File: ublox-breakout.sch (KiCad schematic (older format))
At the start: 43 parts, among them J1 Conn_02x06_Odd_Even, J2 Conn_Coaxial, J3 Conn_Coaxial, J4 USB_B_Micro, U1 74HCT2G125DP,125, U2 UBLOX_LEA-M8T-0, U3 TPUSBLC6-2SC6, U4 XC6206P332MR

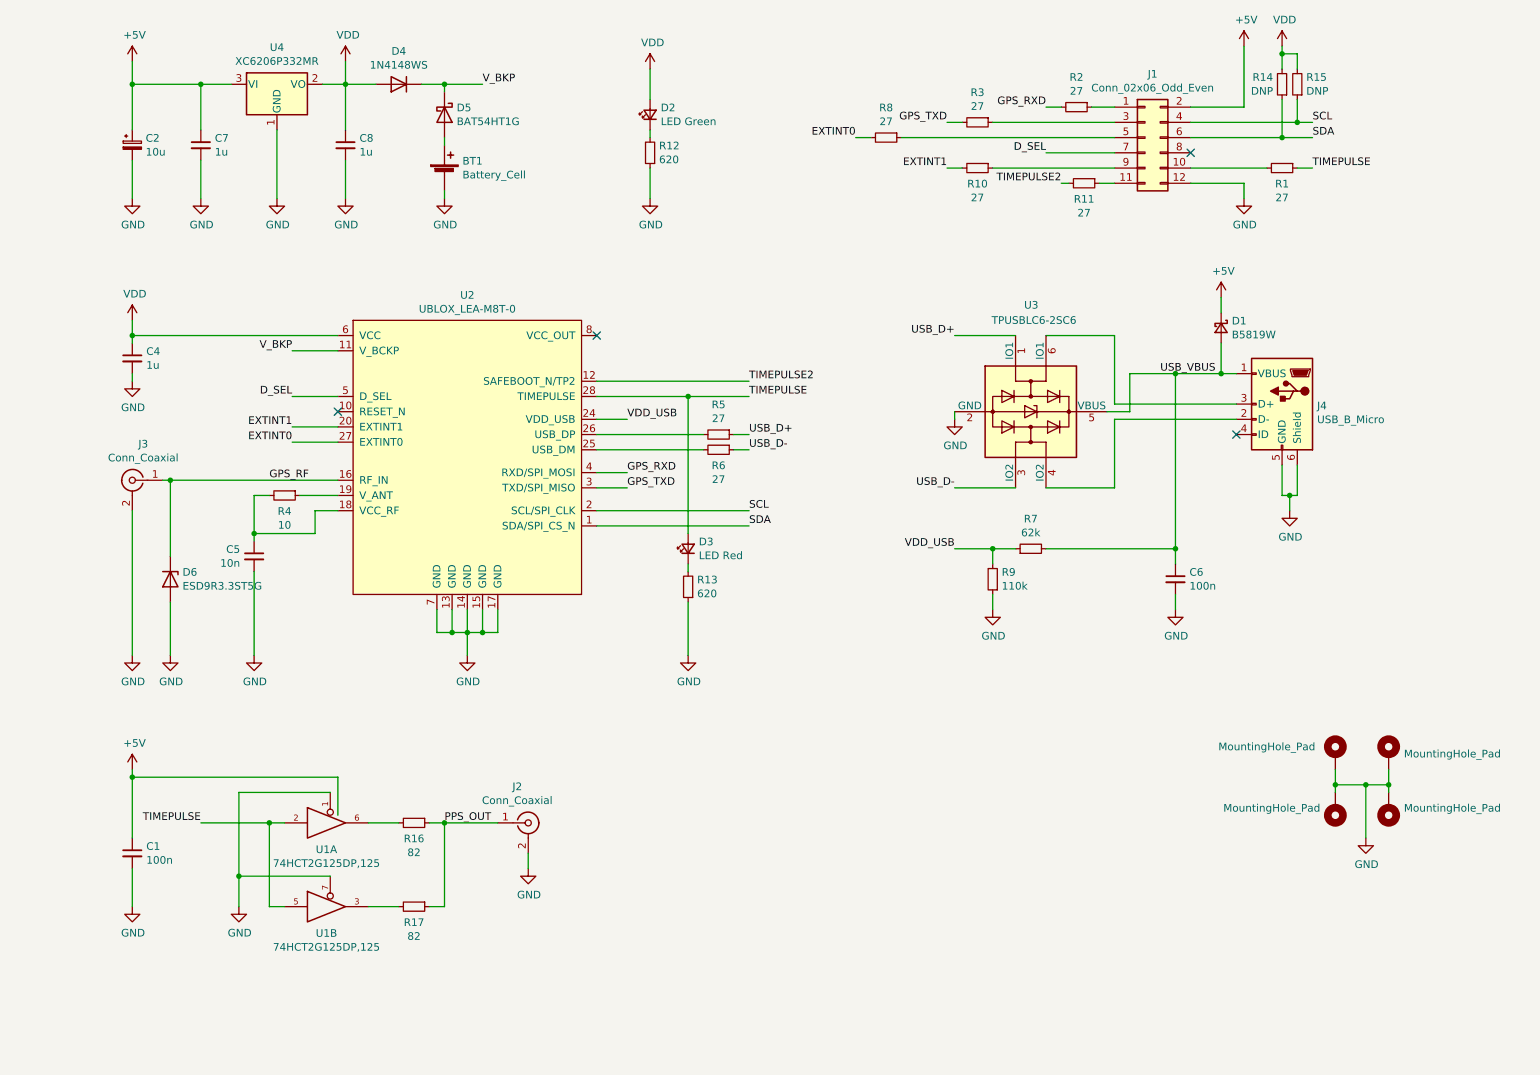
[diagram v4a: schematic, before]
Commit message: Fix USB and other issues
- use an LDO to provide VDD_USB as per HIM (major issue)
- correct trace width for GPS antenna input (minor issue)
- add OSHW logo on top silk
- add copyright notice on top silk
- update gerber, BOM and CPL files
- update schematic PDF
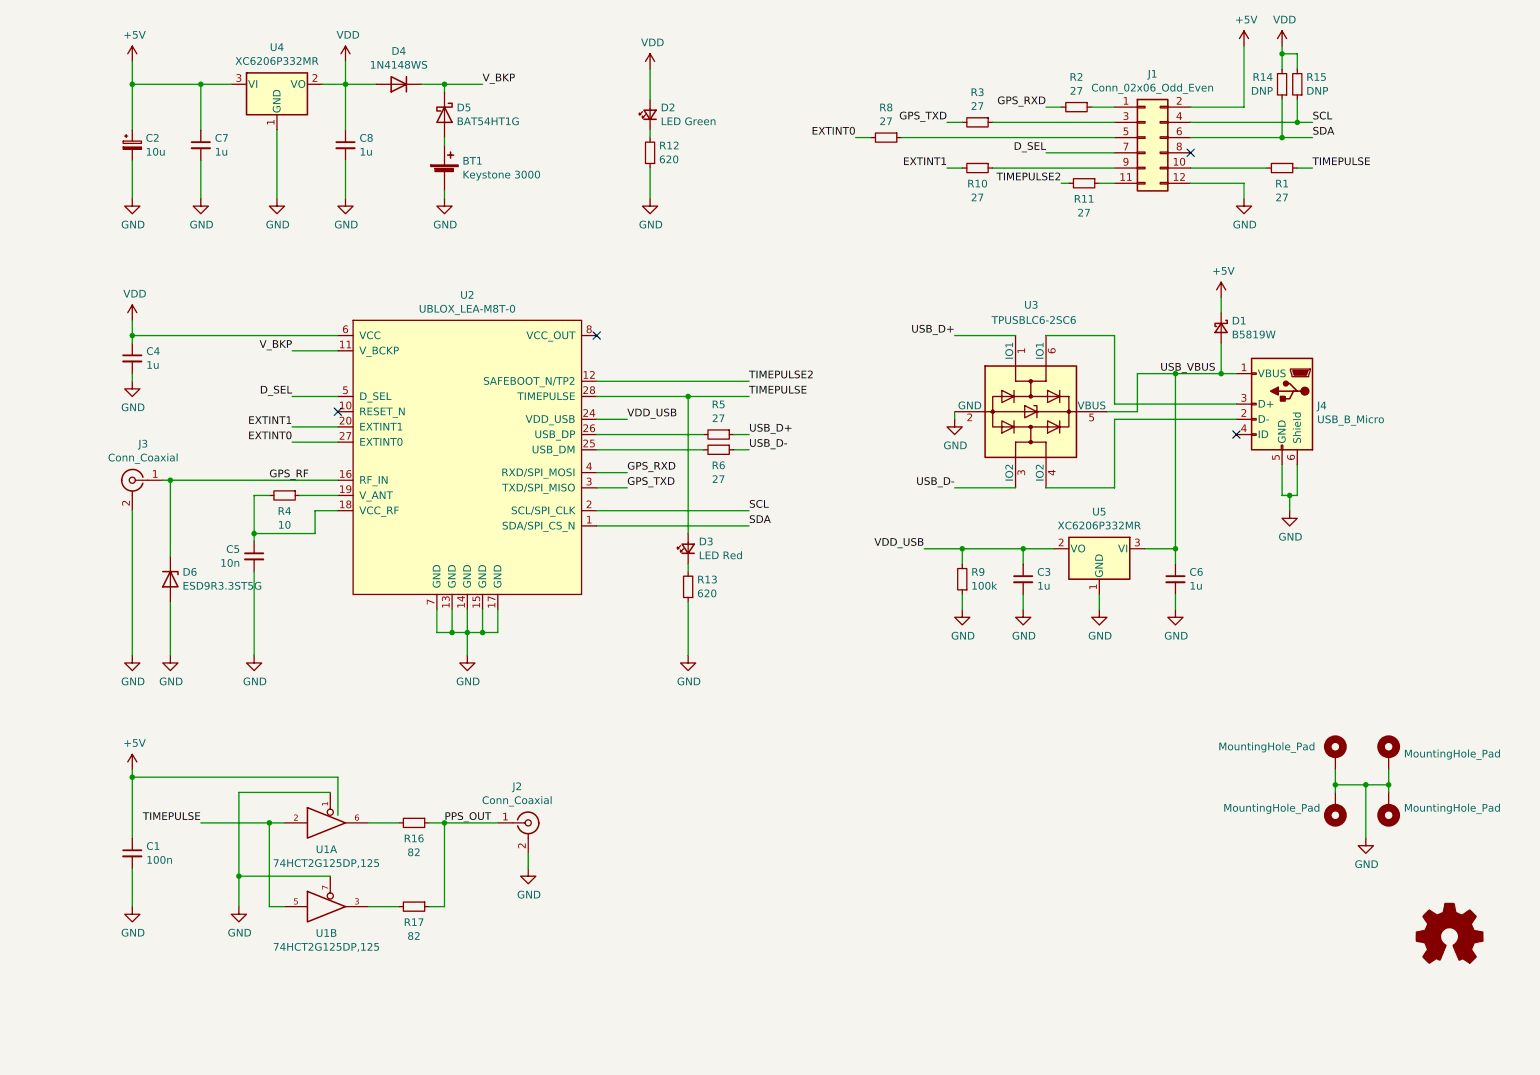
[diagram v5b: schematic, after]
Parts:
- removed R7: 62k, Resistor_SMD:R_0603_1608Metric, symbol Device:R_Small
- added C3: 1u, Capacitor_SMD:C_0603_1608Metric, symbol Device:C_Small
- added OSHW1: Logo_Open_Hardware_Small, Symbol:OSHW-Logo2_9.8x8mm_SilkScreen, symbol Graphic:Logo_Open_Hardware_Small
- added U5: XC6206P332MR, Package_TO_SOT_SMD:SOT-23, symbol Regulator_Linear:XC6206PxxxMR
- BT1: value Battery_Cell -> Keystone 3000
- C6: value 100n -> 1u; JLCPN C14663 -> C15849
- R9: value 110k -> 100k; JLCPN C25805 -> C25803
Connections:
- net GND: now also C3.2, U5.1 (GND)
- net USB_VBUS: now also U5.3 (VI)
- net VDD_USB: now also C3.1, U5.2 (VO)
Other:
- moved on the sheet: R9
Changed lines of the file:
@@
 	9250 3350 8450 3350
 Wire Wire Line
-	8550 3400 8400 3400
-Wire Wire Line
-	8550 3150 8550 3400
+	8600 3400 8400 3400
+Wire Wire Line
+	8600 3150 8600 3400
 Wire Wire Line
 	9250 3150 9150 3150
@@
 L Device:R_Small R9
 U 1 1 5FF28B14
-P 7650 4500
-F 0 "R9" H 7591 4454 50  0000 R CNN
-F 1 "110k" H 7591 4545 50  0000 R CNN
-F 2 "Resistor_SMD:R_0603_1608Metric" H 7650 4500 50  0001 C CNN
-F 3 "~" H 7650 4500 50  0001 C CNN
-F 4 "C25805" H 7650 4500 50  0001 C CNN "JLCPN"
-	1    7650 4500
+P 7450 4500
+F 0 "R9" H 7391 4454 50  0000 R CNN
+F 1 "100k" H 7391 4545 50  0000 R CNN
+F 2 "Resistor_SMD:R_0603_1608Metric" H 7450 4500 50  0001 C CNN
+F 3 "~" H 7450 4500 50  0001 C CNN
+F 4 "C25803" H 7450 4500 50  0001 C CNN "JLCPN"
+	1    7450 4500
 	-1   0    0    1
 $EndComp
-$Comp
-L Device:R_Small R7
-U 1 1 5FF290C8
-P 7900 4300
-F 0 "R7" V 8096 4300 50  0000 C CNN
-F 1 "62k" V 8005 4300 50  0000 C CNN
-F 2 "Resistor_SMD:R_0603_1608Metric" H 7900 4300 50  0001 C CNN
-F 3 "~" H 7900 4300 50  0001 C CNN
-F 4 "C23221" H 7900 4300 50  0001 C CNN "JLCPN"
-	1    7900 4300
-	0    -1   -1   0
-$EndComp
-Wire Wire Line
-	7800 4300 7650 4300
-Wire Wire Line
-	7650 4300 7650 4400
+Wire Wire Line
+	7450 4300 7450 4400
 Wire Wire Line
 	8850 3150 8850 4300
 Wire Wire Line
-	8000 4300 8850 4300
+	8650 4300 8850 4300
 Connection ~ 8850 3150
 Wire Wire Line
-	8850 3150 8550 3150
+	8850 3150 8600 3150
 $Comp
 L power:GND #PWR0101
 U 1 1 5FF37432
-P 7650 4700
-F 0 "#PWR0101" H 7650 4450 50  0001 C CNN
-F 1 "GND" H 7655 4527 50  0000 C CNN
-F 2 "" H 7650 4700 50  0001 C CNN
-F 3 "" H 7650 4700 50  0001 C CNN
-	1    7650 4700
-	1    0    0    -1
-$EndComp
-Wire Wire Line
-	7650 4600 7650 4700
-Wire Wire Line
-	7400 4300 7650 4300
-Connection ~ 7650 4300
-Text Label 7400 4300 2    50   ~ 0
+P 7450 4700
+F 0 "#PWR0101" H 7450 4450 50  0001 C CNN
+F 1 "GND" H 7455 4527 50  0000 C CNN
+F 2 "" H 7450 4700 50  0001 C CNN
+F 3 "" H 7450 4700 50  0001 C CNN
+	1    7450 4700
+	1    0    0    -1
+$EndComp
+Wire Wire Line
+	7450 4600 7450 4700
+Wire Wire Line
+	7200 4300 7450 4300
+Text Label 7200 4300 2    50   ~ 0
 VDD_USB
 $Comp
@@
 P 8850 4500
 F 0 "C6" H 8942 4546 50  0000 L CNN
-F 1 "100n" H 8942 4455 50  0000 L CNN
+F 1 "1u" H 8942 4455 50  0000 L CNN
 F 2 "Capacitor_SMD:C_0603_1608Metric" H 8850 4500 50  0001 C CNN
 F 3 "~" H 8850 4500 50  0001 C CNN
-F 4 "C14663" H 8850 4500 50  0001 C CNN "JLCPN"
+F 4 "C15849" H 8850 4500 50  0001 C CNN "JLCPN"
 	1    8850 4500
 	1    0    0    -1
@@
 P 4050 1850
 F 0 "BT1" H 4168 1946 50  0000 L CNN
-F 1 "Battery_Cell" H 4168 1855 50  0000 L CNN
+F 1 "Keystone 3000" H 4168 1855 50  0000 L CNN
 F 2 "Battery:BatteryHolder_Keystone_3000_1x12mm" V 4050 1910 50  0001 C CNN
 F 3 "~" V 4050 1910 50  0001 C CNN
@@
 Wire Wire Line
 	2450 1250 2000 1250
+$Comp
+L Graphic:Logo_Open_Hardware_Small OSHW1
+U 1 1 5FDCE18C
+P 10650 6850
+F 0 "OSHW1" H 10650 7125 50  0001 C CNN
+F 1 "Logo_Open_Hardware_Small" H 10650 6625 50  0001 C CNN
+F 2 "Symbol:OSHW-Logo2_9.8x8mm_SilkScreen" H 10650 6850 50  0001 C CNN
+F 3 "~" H 10650 6850 50  0001 C CNN
+	1    10650 6850
+	1    0    0    -1
+$EndComp
+$Comp
+L Regulator_Linear:XC6206PxxxMR U5
+U 1 1 5FE83223
+P 8350 4300
+F 0 "U5" H 8350 4542 50  0000 C CNN
+F 1 "XC6206P332MR" H 8350 4451 50  0000 C CNN
+F 2 "Package_TO_SOT_SMD:SOT-23" H 8350 4525 50  0001 C CIN
+F 3 "https://www.torexsemi.com/file/xc6206/XC6206.pdf" H 8350 4300 50  0001 C CNN
+F 4 "C5446" H 8350 4300 50  0001 C CNN "JLCPN"
+	1    8350 4300
+	-1   0    0    -1
+$EndComp
+$Comp
+L power:GND #PWR0121
+U 1 1 5FE9688A
+P 8350 4700
+F 0 "#PWR0121" H 8350 4450 50  0001 C CNN
+F 1 "GND" H 8355 4527 50  0000 C CNN
+F 2 "" H 8350 4700 50  0001 C CNN
+F 3 "" H 8350 4700 50  0001 C CNN
+	1    8350 4700
+	1    0    0    -1
+$EndComp
+Wire Wire Line
+	8350 4600 8350 4700
+$Comp
+L Device:C_Small C3
+U 1 1 5FEA4AF8
+P 7850 4500
+F 0 "C3" H 7942 4546 50  0000 L CNN
+F 1 "1u" H 7942 4455 50  0000 L CNN
+F 2 "Capacitor_SMD:C_0603_1608Metric" H 7850 4500 50  0001 C CNN
+F 3 "~" H 7850 4500 50  0001 C CNN
+F 4 "C15849" H 7850 4500 50  0001 C CNN "JLCPN"
+	1    7850 4500
+	1    0    0    -1
+$EndComp
+$Comp
+L power:GND #PWR0122
+U 1 1 5FEA5100
+P 7850 4700
+F 0 "#PWR0122" H 7850 4450 50  0001 C CNN
+F 1 "GND" H 7855 4527 50  0000 C CNN
+F 2 "" H 7850 4700 50  0001 C CNN
+F 3 "" H 7850 4700 50  0001 C CNN
+	1    7850 4700
+	1    0    0    -1
+$EndComp
+Wire Wire Line
+	7450 4300 7850 4300
+Connection ~ 7450 4300
+Wire Wire Line
+	7850 4300 7850 4400
+Wire Wire Line
+	7850 4600 7850 4700
+Connection ~ 7850 4300
+Wire Wire Line
+	7850 4300 8050 4300
 $EndSCHEMATC

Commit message: USB updates and 1PPS updates
These changes make the USB ESD protection fully optional since the
USBLC6-2SC6 is frequently out of stock at JLCPCB
- replace USBLC6-2SC6 with USBLC6-4SC6
- route a 7mil/4mil differential pair under its body and connect it

Tighter coupling of the 74HCT2G125 buffer to the SMA connector to
bring the impedance closer to 50 Ohm
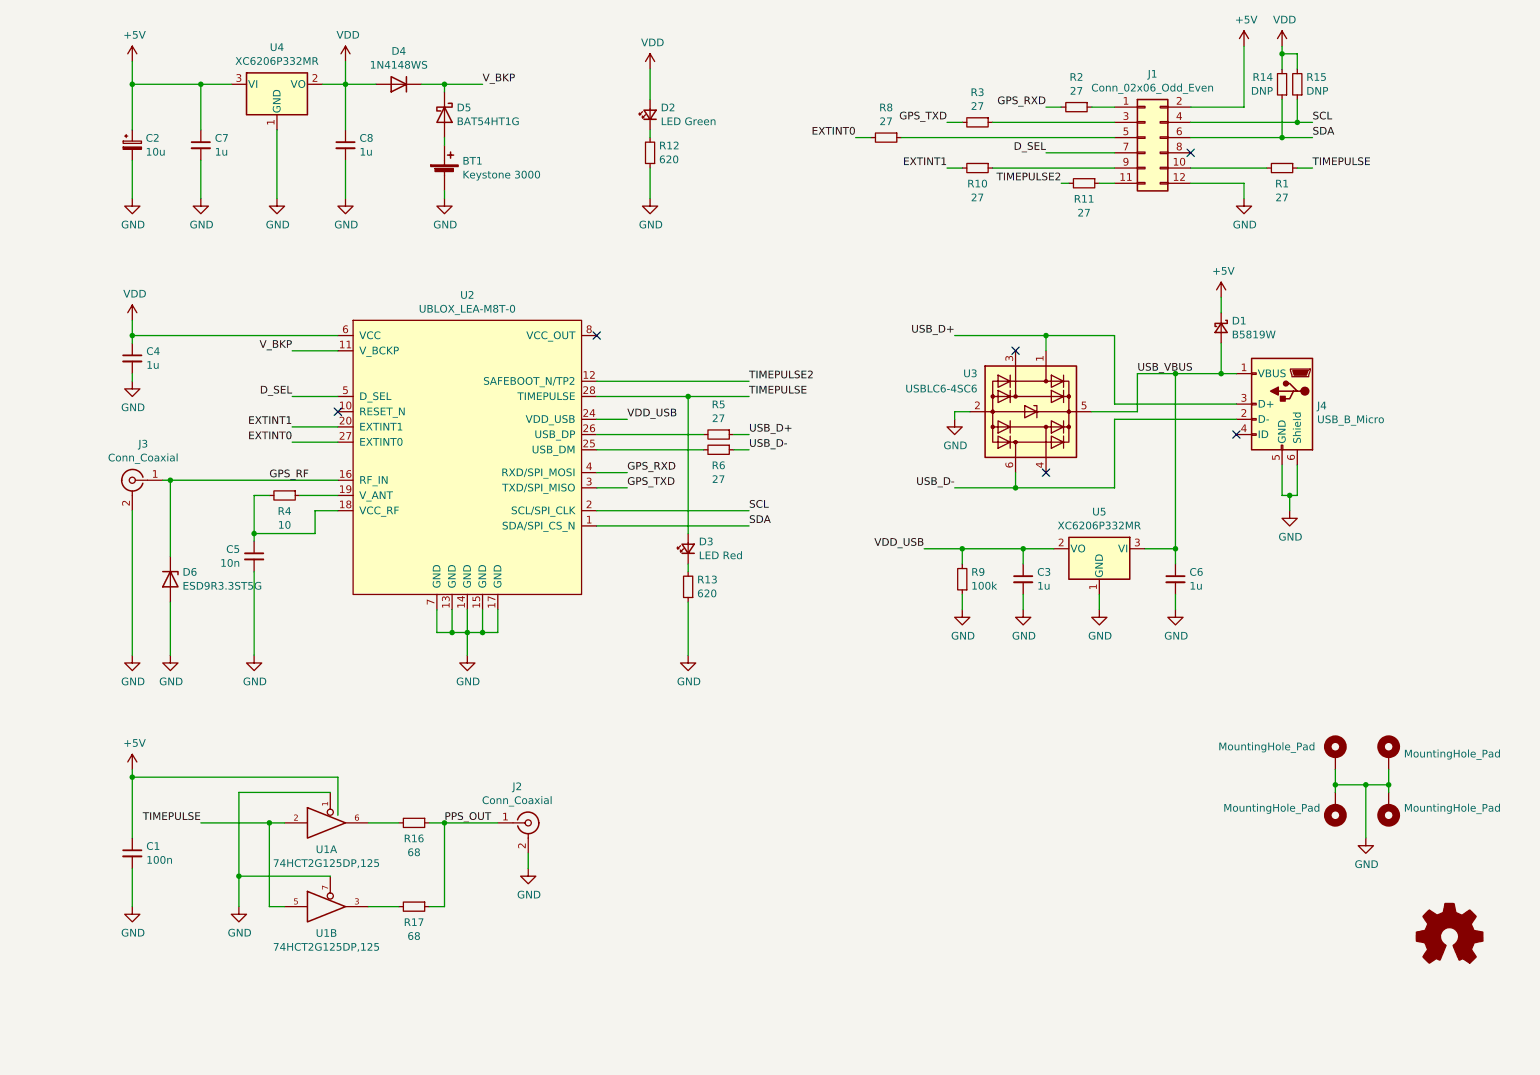
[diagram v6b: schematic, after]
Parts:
- removed U3: TPUSBLC6-2SC6, Package_TO_SOT_SMD:SOT-23-6, symbol ublox-breakout-rescue:USBLC6-2SC6-Power_Protection
- added U3: USBLC6-4SC6, Package_TO_SOT_SMD:SOT-23-6, symbol Power_Protection:USBLC6-4SC6
- R16, R17: value 82 -> 68; JLCPN C23255 -> C27592
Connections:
- net GND: now also U3.2 (GND)
- net USB_D+: now also J4.3 (D+), U3.1 (I/O1)
- net USB_D-: now also J4.2 (D-), U3.6 (I/O4)
- net USB_VBUS: now also U3.5 (VBUS)
- no-connect marks 4 -> 6
